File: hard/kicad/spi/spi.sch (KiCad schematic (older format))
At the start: 9 parts, among them J1 IOx, J2 SPI, SW1 DEVICE, U1 74HC138, U2 74HC174, U3 74HC165, U4 74HC595

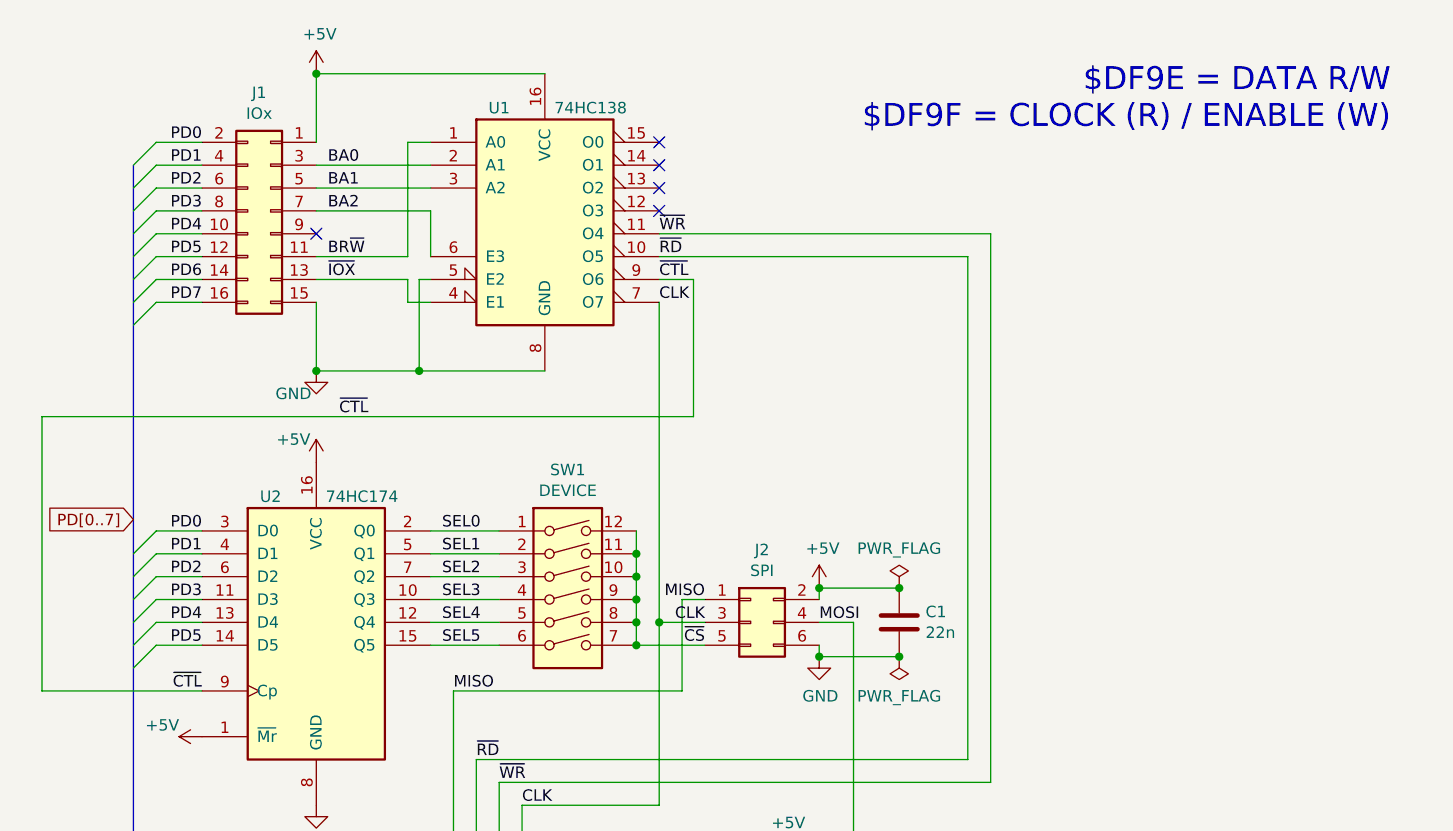
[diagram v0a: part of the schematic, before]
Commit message: finish SPI card
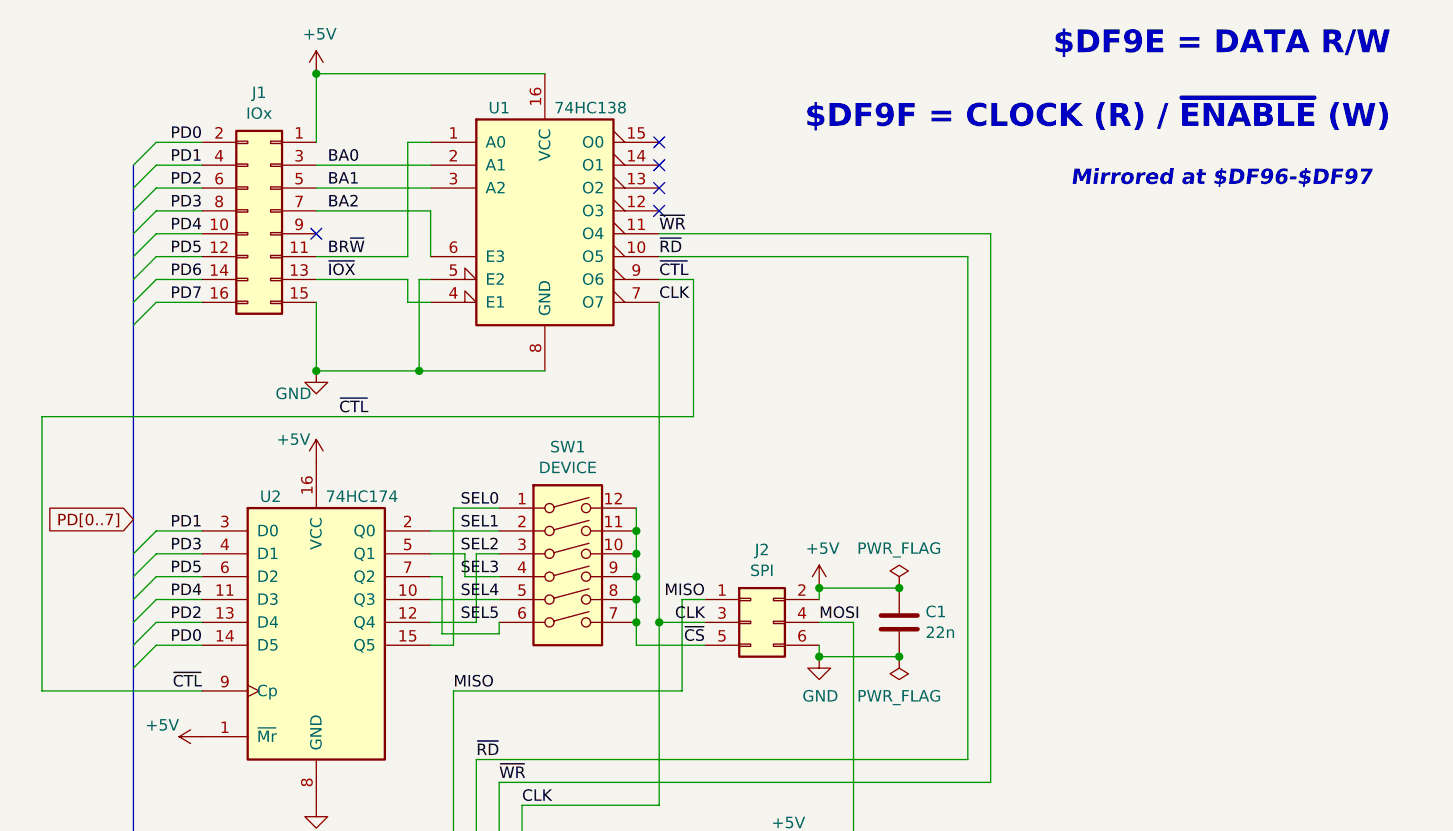
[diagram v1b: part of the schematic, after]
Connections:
- net PD0: now also U2.14 (D5); no longer U2.3 (D0)
- net PD1: now also U2.3 (D0); no longer U2.4 (D1)
- net PD2: now also U2.13 (D4); no longer U2.6 (D2)
- net PD3: now also U2.4 (D1); no longer U2.11 (D3)
- net PD4: now also U2.11 (D3); no longer U2.13 (D4)
- net PD5: now also U2.6 (D2); no longer U2.14 (D5)
- net SEL0: now also U2.15 (Q5); no longer U2.2 (Q0)
- net SEL1: now also U2.2 (Q0); no longer U2.5 (Q1)
- net SEL2: now also U2.12 (Q4); no longer U2.7 (Q2)
- net SEL3: now also U2.5 (Q1); no longer U2.10 (Q3)
- net SEL4: now also U2.10 (Q3); no longer U2.12 (Q4)
- net SEL5: now also U2.7 (Q2); no longer U2.15 (Q5)
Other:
- note added: "$DF9E = DATA R/W\n\n$DF9F = CLOCK (R) / ~ENABLE (W)"
- note added: "Mirrored at $DF96-$DF97"
- note removed: "$DF9E = DATA R/W\n$DF9F = CLOCK (R) / ENABLE (W)"
- moved on the sheet: SW1
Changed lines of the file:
@@
 L Switch:SW_DIP_x06 SW1
 U 1 1 64C433C6
-P 3600 3500
-F 0 "SW1" H 3600 4067 50  0000 C CNN
-F 1 "DEVICE" H 3600 3976 50  0000 C CNN
-F 2 "Package_DIP:DIP-12_W7.62mm" H 3600 3500 50  0001 C CNN
-F 3 "~" H 3600 3500 50  0001 C CNN
-	1    3600 3500
+P 3600 3400
+F 0 "SW1" H 3600 3967 50  0000 C CNN
+F 1 "DEVICE" H 3600 3876 50  0000 C CNN
+F 2 "Package_DIP:DIP-12_W7.62mm" H 3600 3400 50  0001 C CNN
+F 3 "~" H 3600 3400 50  0001 C CNN
+	1    3600 3400
 	1    0    0    -1
 $EndComp
@@
 Entry Wire Line
 	1700 2300 1800 2200
+Text Label 2000 3700 2    50   ~ 0
+PD0
 Text Label 2000 3200 2    50   ~ 0
-PD0
+PD1
+Text Label 2000 3600 2    50   ~ 0
+PD2
 Text Label 2000 3300 2    50   ~ 0
-PD1
+PD3
+Text Label 2000 3500 2    50   ~ 0
+PD4
 Text Label 2000 3400 2    50   ~ 0
-PD2
-Text Label 2000 3500 2    50   ~ 0
-PD3
-Text Label 2000 3600 2    50   ~ 0
-PD4
-Text Label 2000 3700 2    50   ~ 0
 PD5
 Wire Wire Line
@@
 NoConn ~ 2000 5950
 NoConn ~ 5050 5050
-Wire Wire Line
-	3000 3200 3300 3200
-Wire Wire Line
-	3000 3300 3300 3300
-Wire Wire Line
-	3000 3400 3300 3400
-Wire Wire Line
-	3000 3500 3300 3500
-Wire Wire Line
-	3000 3600 3300 3600
-Wire Wire Line
-	3000 3700 3300 3700
-Text Label 3050 3200 0    50   ~ 0
+Text Label 3300 3100 2    50   ~ 0
 SEL0
-Text Label 3050 3300 0    50   ~ 0
+Text Label 3300 3200 2    50   ~ 0
 SEL1
-Text Label 3050 3400 0    50   ~ 0
-SEL2
-Text Label 3050 3500 0    50   ~ 0
+Text Label 3300 3400 2    50   ~ 0
 SEL3
-Text Label 3050 3600 0    50   ~ 0
+Text Label 3300 3500 2    50   ~ 0
 SEL4
-Text Label 3050 3700 0    50   ~ 0
+Text Label 3300 3600 2    50   ~ 0
 SEL5
+Wire Wire Line
+	3900 3100 3900 3200
+Connection ~ 3900 3200
 Wire Wire Line
 	3900 3200 3900 3300
@@
 Wire Wire Line
 	3900 3500 3900 3600
-Connection ~ 3900 3600
-Wire Wire Line
-	3900 3600 3900 3700
-Wire Wire Line
-	3900 3700 4200 3700
-Connection ~ 3900 3700
 Text Label 4200 3700 2    50   ~ 0
 ~CS
@@
 Wire Wire Line
 	3400 4400 3400 5550
-Wire Bus Line
-	3750 5150 3750 6250
-Wire Bus Line
-	1700 1600 1700 6250
 Connection ~ 4000 3600
 Connection ~ 3400 5550
@@
 Text Label 2600 2700 0    50   ~ 0
 ~CTL
-Text Notes 7200 1450 2    100  ~ 0
-$DF9E = DATA R/W\n$DF9F = CLOCK (R) / ENABLE (W)
+Text Notes 7200 1450 2    100  ~ 20
+$DF9E = DATA R/W\n\n$DF9F = CLOCK (R) / ~ENABLE (W)
 $Comp
 L Graphic:Logo_Open_Hardware_Small LOGO1
@@
 	1    0    0    -1
 $EndComp
+Wire Wire Line
+	3300 3100 3100 3100
+Wire Wire Line
+	3100 3700 3000 3700
+Wire Wire Line
+	3000 3200 3300 3200
+Wire Wire Line
+	3100 3100 3100 3700
+Wire Wire Line
+	3900 3600 3900 3700
+Wire Wire Line
+	3900 3700 4200 3700
+Connection ~ 3900 3600
+Wire Wire Line
+	3200 3300 3200 3600
+Wire Wire Line
+	3200 3600 3000 3600
+Wire Wire Line
+	3000 3300 3150 3300
+Wire Wire Line
+	3150 3300 3150 3400
+Wire Wire Line
+	3150 3400 3300 3400
+Wire Wire Line
+	3300 3300 3200 3300
+Text Label 3300 3300 2    50   ~ 0
+SEL2
+Wire Wire Line
+	3300 3500 3000 3500
+Wire Wire Line
+	3000 3400 3050 3400
+Wire Wire Line
+	3050 3400 3050 3650
+Wire Wire Line
+	3050 3650 3300 3650
+Wire Wire Line
+	3300 3650 3300 3600
+Wire Bus Line
+	3750 5150 3750 6250
+Wire Bus Line
+	1700 1600 1700 6250
+Text Notes 5800 1700 0    67   Italic 13
+Mirrored at $DF96-$DF97
 $EndSCHEMATC

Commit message: update values in clock divider
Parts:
- added C2, C3: 68p, symbol Device:C
- added C4: 470p, symbol Device:C
- added D1, D2, D3, D4, D5: 1N4148, symbol Device:D
- added R1: 1K2, symbol Device:R
- added R2, R3, R4: 3K3, symbol Device:R
- added R5: 6K8, symbol Device:R
- added U5: 74HC14, symbol 74xx:74LS14
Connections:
- net +5V: now also D5.1 (K), R1.1, R5.1
- net CLK: now also C3.2; no longer J2.3 (Pin_3), U4.11 (SRCLK), U4.12 (RCLK)
- net GND: now also D1.2 (A), D2.2 (A), R2.2, R3.2, U5.7 (GND)
- net ~WR: now also C2.2
- new net: U5.13, U5.14 (VCC)
- new net D_CLK: C3.1, D2.1 (K), R3.1, U5.3
- new net D_SCK: C4.1, D5.2 (A), R5.2, U5.11
- new net D_WR: C2.1, D1.1 (K), R2.1, U5.1
- new net OCLK: U4.11 (SRCLK), U4.12 (RCLK), U5.8
- new net R_AND: D3.2 (A), D4.2 (A), R1.2, R4.2
- new net R_CLK: D4.1 (K), U5.4
- new net R_DLY: R4.1, U5.5
- new net R_WR: D3.1 (K), U5.2
- new net SCLK: C4.2, J2.3 (Pin_3), U5.6
- new net ~OCLK: U5.10, U5.9
- no-connect marks 7 -> 8
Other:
- moved on the sheet: C1, J2

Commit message: add alternative clock-splitting circuit
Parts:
- added C2, C3, C4: 68p, symbol Device:C
- added D1, D2, D3: 1N4148, symbol Device:D
- added Q1: 2N7000, digikey-footprints:TO-92-3, symbol dk_Transistors-FETs-MOSFETs-Single:2N7000
- added R1: 1K2, symbol Device:R
- added R2, R3, R4: 3K3, symbol Device:R
- added R5: 6K8, symbol Device:R
- added U5: 74HC132, symbol 74xx:74LS132
- C4: value 470p -> 68p
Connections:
- net +5V: now also R1.1; no longer D5.1 (K), R5.1
- net CLK: now also C3.2
- net D_CLK: now also C3.1, D2.1 (K), R3.1, U5.4, U5.5
- net D_SCK: now also D5.1 (K), R5.1, U5.9, C4.1, D3.1 (K), R5.1, U5.10, U5.9; no longer D5.2 (A), R5.2, U5.11
- net D_WR: now also C2.1, D1.1 (K), R2.1, U5.1, U5.2
- net GND: now also D5.2 (A), R5.2, D1.2 (A), D2.2 (A), D3.2 (A), Q1.1 (S), R2.2, R3.2, R5.2
- net OCLK: now also U5.8
- net R_CLK: now also R4.2, U5.6
- net R_DLY: now also R4.1, U5.13
- net R_WR: now also U5.12, U5.3
- net SCLK: now also U5.11, Q1.2 (G), U5.11; no longer C4.2
- net ~WR: now also C2.2
- net ~OCLK renamed ~SCLK
- net ~SCLK: now also C4.2, C4.2, Q1.3 (D), R1.2; no longer U5.9
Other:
- note added: "Alternative circuit"
- note added: "U5 *must* be 74HC14,\nnot 74HCT, not 74AC"
- moved on the sheet: C4, D5, R5, U5E

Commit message: minor renaming in SPI
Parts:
- C10: renamed from C2; footprint (none) -> Capacitor_THT:C_Disc_D3.8mm_W2.6mm_P2.50mm
- C11: renamed from C3; footprint (none) -> Capacitor_THT:C_Disc_D3.8mm_W2.6mm_P2.50mm
- C12: renamed from C4; footprint (none) -> Capacitor_THT:C_Disc_D3.8mm_W2.6mm_P2.50mm
- C2, C3, C4: footprint (none) -> Capacitor_THT:C_Disc_D3.8mm_W2.6mm_P2.50mm
- D1, D2, D3, D4, D5: footprint (none) -> Diode_THT:D_DO-35_SOD27_P2.54mm_Vertical_AnodeUp
- D10: renamed from D1; footprint (none) -> Diode_THT:D_DO-35_SOD27_P2.54mm_Vertical_AnodeUp
- D11: renamed from D2; footprint (none) -> Diode_THT:D_DO-35_SOD27_P2.54mm_Vertical_AnodeUp
- D12: renamed from D3; footprint (none) -> Diode_THT:D_DO-35_SOD27_P2.54mm_Vertical_AnodeUp
- R1, R2, R3, R4, R5: footprint (none) -> Resistor_THT:R_Axial_DIN0207_L6.3mm_D2.5mm_P2.54mm_Vertical
- R10: renamed from R2; footprint (none) -> Resistor_THT:R_Axial_DIN0207_L6.3mm_D2.5mm_P2.54mm_Vertical
- R11: renamed from R3; footprint (none) -> Resistor_THT:R_Axial_DIN0207_L6.3mm_D2.5mm_P2.54mm_Vertical
- R12: renamed from R5; footprint (none) -> Resistor_THT:R_Axial_DIN0207_L6.3mm_D2.5mm_P2.54mm_Vertical
- R13: renamed from R4; footprint (none) -> Resistor_THT:R_Axial_DIN0207_L6.3mm_D2.5mm_P2.54mm_Vertical
- R14: renamed from R1; footprint (none) -> Resistor_THT:R_Axial_DIN0207_L6.3mm_D2.5mm_P2.54mm_Vertical
- U10: renamed from U5; footprint (none) -> Package_DIP:DIP-14_W7.62mm_Socket
- U5: footprint (none) -> Package_DIP:DIP-14_W7.62mm_Socket
- renumbered Q1 to Q10
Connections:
- net +5V: now also U5.13, U5.14 (VCC)

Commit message: finish Fast SPI card
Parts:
- removed C2, C3, C4: 68p, Capacitor_THT:C_Disc_D3.8mm_W2.6mm_P2.50mm, symbol Device:C
- removed D1, D2, D3, D4, D5: 1N4148, Diode_THT:D_DO-35_SOD27_P2.54mm_Vertical_AnodeUp, symbol Device:D
- removed R1: 1K2, Resistor_THT:R_Axial_DIN0207_L6.3mm_D2.5mm_P2.54mm_Vertical, symbol Device:R
- removed R2, R3, R4: 3K3, Resistor_THT:R_Axial_DIN0207_L6.3mm_D2.5mm_P2.54mm_Vertical, symbol Device:R
- removed R5: 6K8, Resistor_THT:R_Axial_DIN0207_L6.3mm_D2.5mm_P2.54mm_Vertical, symbol Device:R
- removed SW1: DEVICE, Package_DIP:DIP-12_W7.62mm, symbol Switch:SW_DIP_x06
- removed U5: 74HC14, Package_DIP:DIP-14_W7.62mm_Socket, symbol 74xx:74LS14
- added J3: SPI 1, Connector_IDC:IDC-Header_2x03_P2.54mm_Vertical, symbol Connector_Generic:Conn_02x03_Odd_Even
- added J4: SPI 2, Connector_IDC:IDC-Header_2x03_P2.54mm_Vertical, symbol Connector_Generic:Conn_02x03_Odd_Even
- added J5: SPI 3, Connector_IDC:IDC-Header_2x03_P2.54mm_Vertical, symbol Connector_Generic:Conn_02x03_Odd_Even
- added J6: SPI 4, Connector_IDC:IDC-Header_2x03_P2.54mm_Vertical, symbol Connector_Generic:Conn_02x03_Odd_Even
- added J7: SPI 5, Connector_IDC:IDC-Header_2x03_P2.54mm_Vertical, symbol Connector_Generic:Conn_02x03_Odd_Even
- added unit 5 of U5
- D1: renamed from D10; value 1N4148 -> 4148
- D2: renamed from D11; value 1N4148 -> 4148
- D3: renamed from D12; value 1N4148 -> 4148
- J2: value SPI -> SPI 0
- renumbered C10 to C2, C11 to C3, C12 to C4, Q10 to Q1, R14 to R1, R10 to R2, R11 to R3, R12 to R4, R13 to R5, U10 to U5
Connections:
- net ~CS is gone; now on net SEL0: J2.5 (Pin_5)
- net +5V: now also J3.2 (Pin_2), J4.2 (Pin_2), J5.2 (Pin_2), J6.2 (Pin_2), J7.2 (Pin_2), U5.14 (VCC)
- net GND: now also J3.6 (Pin_6), J4.6 (Pin_6), J5.6 (Pin_6), J6.6 (Pin_6), J7.6 (Pin_6), U5.7 (GND)
- net MISO: now also J3.1 (Pin_1), J4.1 (Pin_1), J5.1 (Pin_1), J6.1 (Pin_1), J7.1 (Pin_1)
- net MOSI: now also J3.4 (Pin_4), J4.4 (Pin_4), J5.4 (Pin_4), J6.4 (Pin_4), J7.4 (Pin_4)
- net SCLK: now also J3.3 (Pin_3), J4.3 (Pin_3), J5.3 (Pin_3), J6.3 (Pin_3), J7.3 (Pin_3)
- net SEL1: now also J3.5 (Pin_5)
- net SEL2: now also J4.5 (Pin_5)
- net SEL3: now also J5.5 (Pin_5)
- net SEL4: now also J6.5 (Pin_5)
- net SEL5: now also J7.5 (Pin_5)
- no-connect marks 8 -> 7
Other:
- note removed: "Alternative circuit"
- note removed: "U5 *must* be 74HC14,\nnot 74HCT, not 74AC"
- moved on the sheet: C1, C2, C3, C4, D1, D2, D3, J2, Q1, R1, R2, R3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

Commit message: last non-I2C SPI board
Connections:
- net GND: no longer U1.5 (E2)
- net BA3: now reaches J1.9 (Pin_9)
- net BA3: now also U1.5 (E2)
- no-connect marks 7 -> 6
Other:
- note added: "$DF96 = DATA R/W\n\n$DF97 = CLOCK (R) / ~ENABLE (W)"
- note removed: "$DF9E = DATA R/W\n\n$DF9F = CLOCK (R) / ~ENABLE (W)"
- note removed: "Mirrored at $DF96-$DF97"
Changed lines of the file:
@@
 	3000 1800 3000 2000
 Wire Wire Line
-	3000 2100 2950 2100
-Wire Wire Line
-	2950 2100 2950 2500
-Wire Wire Line
-	2950 2500 3500 2500
-Wire Wire Line
 	2500 2100 2900 2100
 Wire Wire Line
@@
 Wire Wire Line
 	2500 2200 2500 2500
-Wire Wire Line
-	2500 2500 2950 2500
-Connection ~ 2950 2500
 Wire Wire Line
 	2500 1500 2500 1200
@@
 Text Label 2550 2100 0    50   ~ 0
 ~IOX
-NoConn ~ 2500 1900
 Text Label 2000 1500 2    50   ~ 0
 PD0
@@
 ~CTL
 Text Notes 6300 1250 2    100  ~ 20
-$DF9E = DATA R/W\n\n$DF9F = CLOCK (R) / ~ENABLE (W)
+$DF96 = DATA R/W\n\n$DF97 = CLOCK (R) / ~ENABLE (W)
 $Comp
 L Graphic:Logo_Open_Hardware_Small LOGO1
@@
 Wire Wire Line
 	3000 3400 9600 3400
-Text Notes 4300 1450 0    67   Italic 13
-Mirrored at $DF96-$DF97
 Wire Wire Line
 	3650 4800 3650 6150
@@
 Wire Wire Line
 	5600 3200 3000 3200
+Wire Wire Line
+	2500 2500 3500 2500
+Wire Wire Line
+	2500 1900 2950 1900
+Wire Wire Line
+	2950 1900 2950 2100
+Wire Wire Line
+	2950 2100 3000 2100
 Wire Bus Line
 	3750 5150 3750 6250
 Wire Bus Line
 	1700 1600 1700 6250
+Text Label 2550 1900 0    50   ~ 0
+BA3
 $EndSCHEMATC

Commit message: almost ready FastSPI+I2C
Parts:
- removed J6: SPI 4, Connector_IDC:IDC-Header_2x03_P2.54mm_Vertical, symbol Connector_Generic:Conn_02x03_Odd_Even
- removed J7: SPI 5, Connector_IDC:IDC-Header_2x03_P2.54mm_Vertical, symbol Connector_Generic:Conn_02x03_Odd_Even
- added U6: 74HC245, Package_DIP:DIP-20_W7.62mm_Socket, symbol 74xx:74HC245
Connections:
- net +5V: now also U6.1 (A->B), U6.20 (VCC)
- net GND: now also U6.10 (GND)
- net PD0: now also U6.18 (B0)
- net PD1: now also U6.17 (B1)
- net PD2: now also U6.16 (B2)
- net PD3: now also U6.15 (B3)
- net PD4: now also U6.14 (B4)
- net PD5: now also U6.13 (B5)
- net PD6: now also U6.12 (B6)
- net PD7: now also U6.11 (B7)
- net SEL0 renamed ~CS0
- net ~CS0: now also U6.2 (A0)
- net SEL1 renamed ~CS1
- net ~CS1: now also U6.3 (A1)
- net SEL2 renamed ~CS2
- net ~CS2: now also U6.4 (A2)
- net SEL3 renamed ~CS3
- net ~CS3: now also U6.5 (A3)
- net SEL4 renamed SCL
- net SCL: now also U6.6 (A4)
- net SEL5 renamed SDA
- net SDA: now also U6.7 (A5)
- new net I2C_C: U6.8 (A6)
- new net I2C_D: U6.9 (A7)
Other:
- note added: "$DF96 = SPI DATA R/W\n\n$DF97 (R) = SPI CLOCK, D0..3: SPI ~ENABLE~, D6: I2C_SCL, D7: I2C_SDA\n$DF97 (W) = D0..3: SPI ~ENABLE~, D4: I2C_SCL, D5: I2C_SDA"
- note removed: "$DF96 = DATA R/W\n\n$DF97 = CLOCK (R) / ~ENABLE (W)"
- moved on the sheet: C2, C3, C4, D1, D2, D3, Q1, R1, R2, R3, R4, R5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

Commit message: finish FastSPI+I2C
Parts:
- added D4, D5: BAT85, Diode_THT:D_DO-35_SOD27_P2.54mm_Vertical_KathodeUp, symbol Device:D
- added J6: I2C, Connector_PinHeader_2.54mm:PinHeader_1x05_P2.54mm_Horizontal, symbol Connector_Generic:Conn_01x05
- added R6, R7: 3K3, Resistor_THT:R_Axial_DIN0207_L6.3mm_D2.5mm_P2.54mm_Vertical, symbol Device:R
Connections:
- net +5V: now also J6.5 (Pin_5), R6.1, R7.1
- net GND: now also J6.1 (Pin_1)
- net I2C_C: now also D4.1 (K), J6.2 (Pin_2), R6.2
- net I2C_D: now also D5.1 (K), J6.3 (Pin_3), R7.2
- net SCL: now also D4.2 (A)
- net SDA: now also D5.2 (A)
- no-connect marks 6 -> 7
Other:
- moved on the sheet: U6
